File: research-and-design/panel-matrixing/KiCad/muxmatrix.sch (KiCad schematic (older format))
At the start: 112 parts, among them P1 CONN_01X03, P10 CONN_01X03, P11 CONN_01X03, P12 CONN_01X03, P13 CONN_01X03, P14 CONN_01X03, P15 CONN_01X03, P16 CONN_01X03, P17 CONN_01X03, P18 CONN_01X03, P19 CONN_01X03, P2 CONN_01X03, P20 CONN_01X03, P21 CONN_01X07, P22 CONN_01X03, P23 CONN_01X03, P24 CONN_01X03, P25 CONN_01X03, P26 CONN_01X03, P27 CONN_01X03, P28 CONN_01X03, P29 CONN_01X03, P3 CONN_01X03, P30 CONN_01X03, P31 CONN_01X03, P32 CONN_01X03, P33 CONN_01X03, P4 CONN_01X03, P5 CONN_01X03, P6 CONN_01X03, P7 CONN_01X03, P8 CONN_01X03, P9 CONN_01X03, U1 4052, U10 4052, U2 4052, U3 4052, U4 4052, U5 4052, U6 4052, U7 4052, U8 4052, U9 4052

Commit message: worked on layout
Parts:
- removed U10, U2, U4, U6, U8: 4052, SMD_Packages:SO-16-L, symbol 4052
- U1: footprint SMD_Packages:SO-16-L -> SMD_Packages:SO-16-N
- U2: renamed from U5; footprint SMD_Packages:SO-16-L -> SMD_Packages:SO-16-N
- U3: renamed from U7; footprint SMD_Packages:SO-16-L -> SMD_Packages:SO-16-N
- U4: renamed from U9; footprint SMD_Packages:SO-16-L -> SMD_Packages:SO-16-N
- U5: renamed from U3; footprint SMD_Packages:SO-16-L -> SMD_Packages:SO-16-N
- renumbered P19 to P10, P22 to P11, P24 to P12, P26 to P13, P28 to P14, P30 to P15, P32 to P16, P2 to P17, P4 to P18, P6 to P19, P3 to P2, P8 to P20, P10 to P21, P12 to P22, P14 to P23, P16 to P24, P18 to P25, P20 to P26, P23 to P27, P25 to P28, P27 to P29, P5 to P3, P29 to P30, P33 to P32, P21 to P33, P7 to P4, P9 to P5, P11 to P6, P13 to P7, P15 to P8, P17 to P9, R37 to R10, R41 to R11, R45 to R12, R49 to R13, R53 to R14, R57 to R15, R61 to R16, R2 to R17, R6 to R18, R10 to R19, R5 to R2, R14 to R20, R18 to R21, R26 to R23, R30 to R24, R34 to R25, R38 to R26, R42 to R27, R46 to R28, R50 to R29, R9 to R3, R54 to R30, R58 to R31, R62 to R32, R3 to R33, R7 to R34, R11 to R35, R15 to R36, R19 to R37, R23 to R38, R27 to R39, R13 to R4, R31 to R40, R35 to R41, R39 to R42, R47 to R44, R51 to R45, R55 to R46, R59 to R47, R63 to R48, R4 to R49, R17 to R5, R8 to R50, R12 to R51, R16 to R52, R20 to R53, R24 to R54, R28 to R55, R32 to R56, R36 to R57, R40 to R58, R44 to R59, R21 to R6, R48 to R60, R52 to R61, R56 to R62, R60 to R63, R25 to R7, R29 to R8, R33 to R9

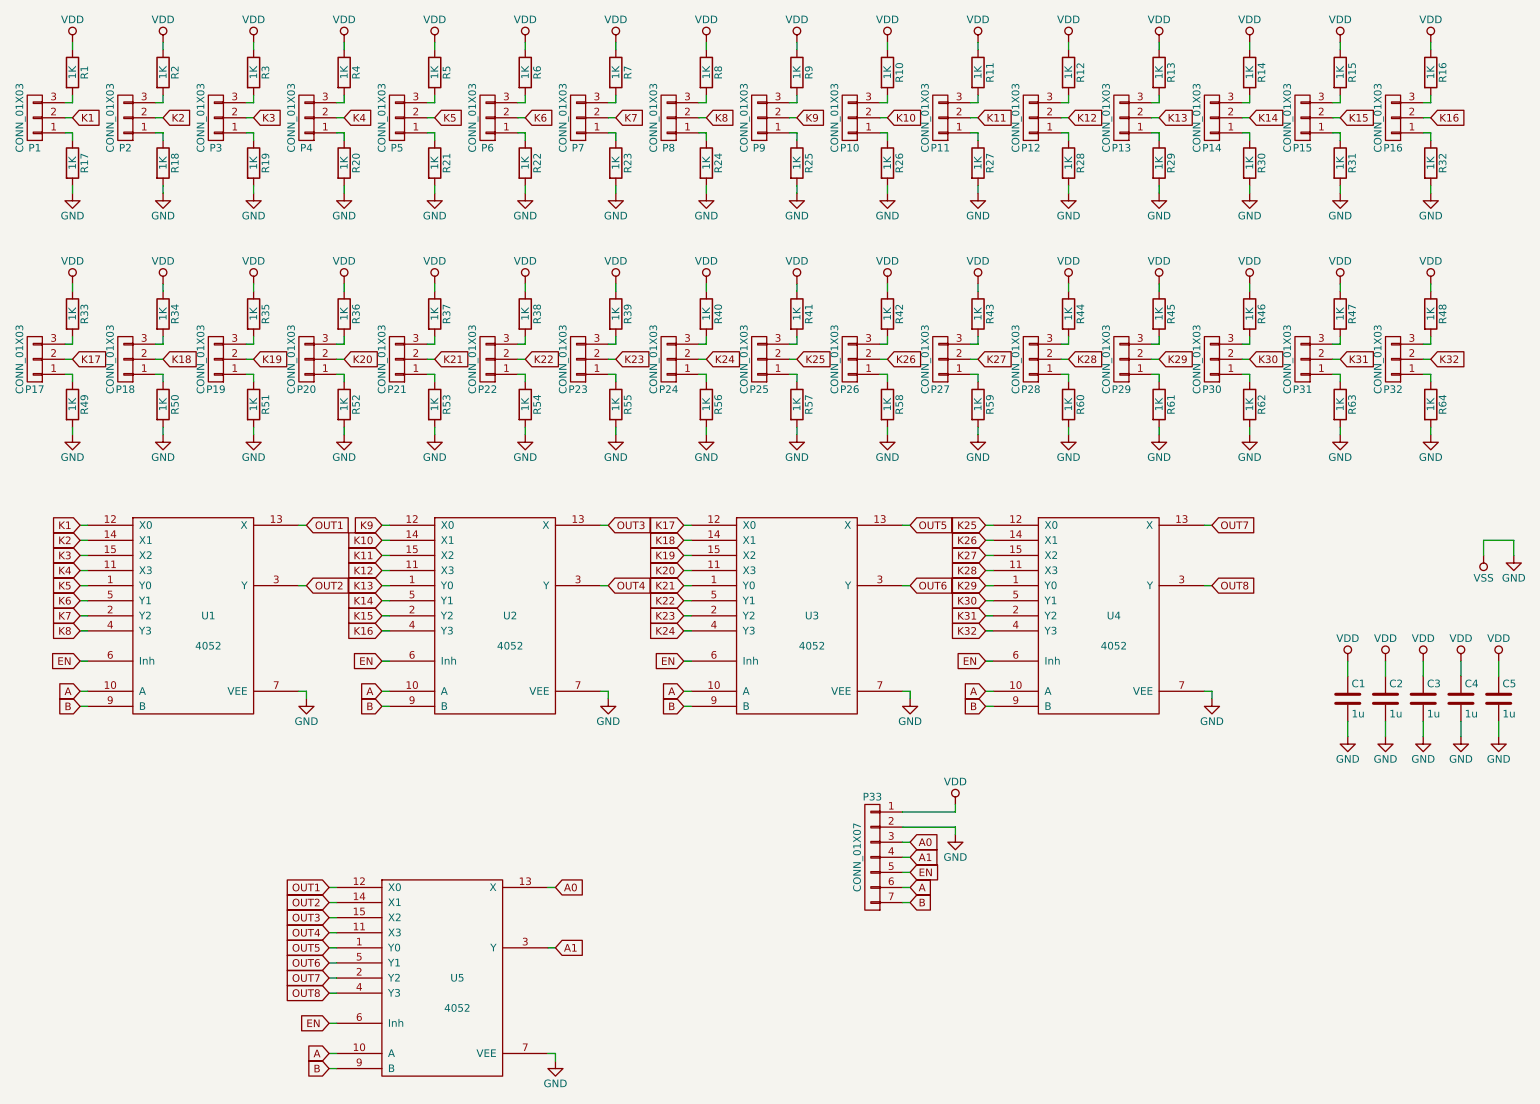
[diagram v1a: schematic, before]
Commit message: Testing out new dual trimpot footprint
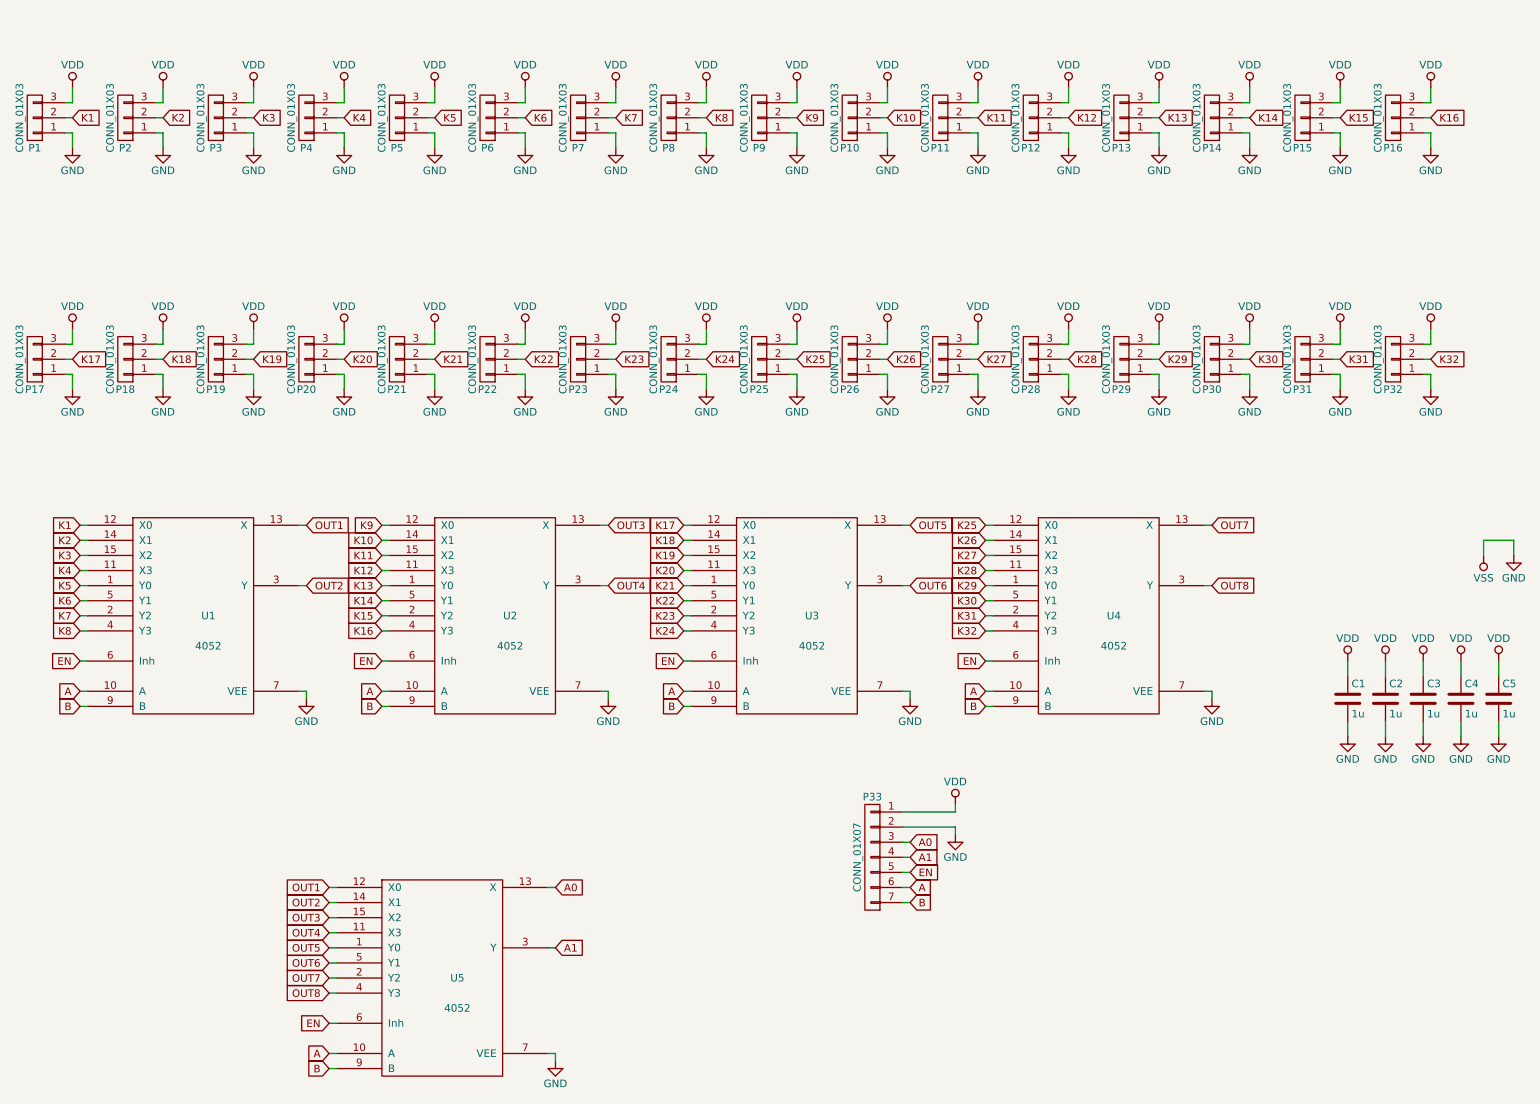
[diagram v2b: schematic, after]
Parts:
- removed R1, R10, R11, R12, R13, R14, R15, R16, R17, R18, R19, R2, R20, R21, R22, R23, R24, R25, R26, R27, R28, R29, R3, R30, R31, R32, R33, R34, R35, R36, R37, R38, R39, R4, R40, R41, R42, R43, R44, R45, R46, R47, R48, R49, R5, R50, R51, R52, R53, R54, R55, R56, R57, R58, R59, R6, R60, R61, R62, R63, R64, R7, R8, R9: 1K, Resistors_SMD:R_0603, symbol R
- P1, P10, P11, P12, P13, P14, P15, P16, P17, P18, P19, P2, P20, P21, P22, P23, P24, P25, P26, P27, P28, P29, P3, P30, P31, P32, P4, P5, P6, P7, P8, P9: footprint Pin_Headers:Pin_Header_Straight_1x03 -> trytwo:dualpot
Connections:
- net GND: now also P1.1 (P1), P10.1 (P1), P11.1 (P1), P12.1 (P1), P13.1 (P1), P14.1 (P1), P15.1 (P1), P16.1 (P1), P17.1 (P1), P18.1 (P1), P19.1 (P1), P2.1 (P1), P20.1 (P1), P21.1 (P1), P22.1 (P1), P23.1 (P1), P24.1 (P1), P25.1 (P1), P26.1 (P1), P27.1 (P1), P28.1 (P1), P29.1 (P1), P3.1 (P1), P30.1 (P1), P31.1 (P1), P32.1 (P1), P4.1 (P1), P5.1 (P1), P6.1 (P1), P7.1 (P1), P8.1 (P1), P9.1 (P1)
- net VDD: now also P1.3 (P3), P10.3 (P3), P11.3 (P3), P12.3 (P3), P13.3 (P3), P14.3 (P3), P15.3 (P3), P16.3 (P3), P17.3 (P3), P18.3 (P3), P19.3 (P3), P2.3 (P3), P20.3 (P3), P21.3 (P3), P22.3 (P3), P23.3 (P3), P24.3 (P3), P25.3 (P3), P26.3 (P3), P27.3 (P3), P28.3 (P3), P29.3 (P3), P3.3 (P3), P30.3 (P3), P31.3 (P3), P32.3 (P3), P4.3 (P3), P5.3 (P3), P6.3 (P3), P7.3 (P3), P8.3 (P3), P9.3 (P3)
